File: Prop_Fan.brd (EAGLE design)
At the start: 160 x 100 mm, 77 parts, among them J1 500075-1517, SW1 EVQ-Q2203W, U1 P8X32A, U10 MAX31855KASA+, U2 FT230X, U3 LM22678TJ-5.0/NOPB, U6 ADP3338AKCZ-3.3-RL, U8 CAT24C512WI-GT3, U9 MAX31855KASA+, X1 ABLS3-6.000MHZ-D4Y-T

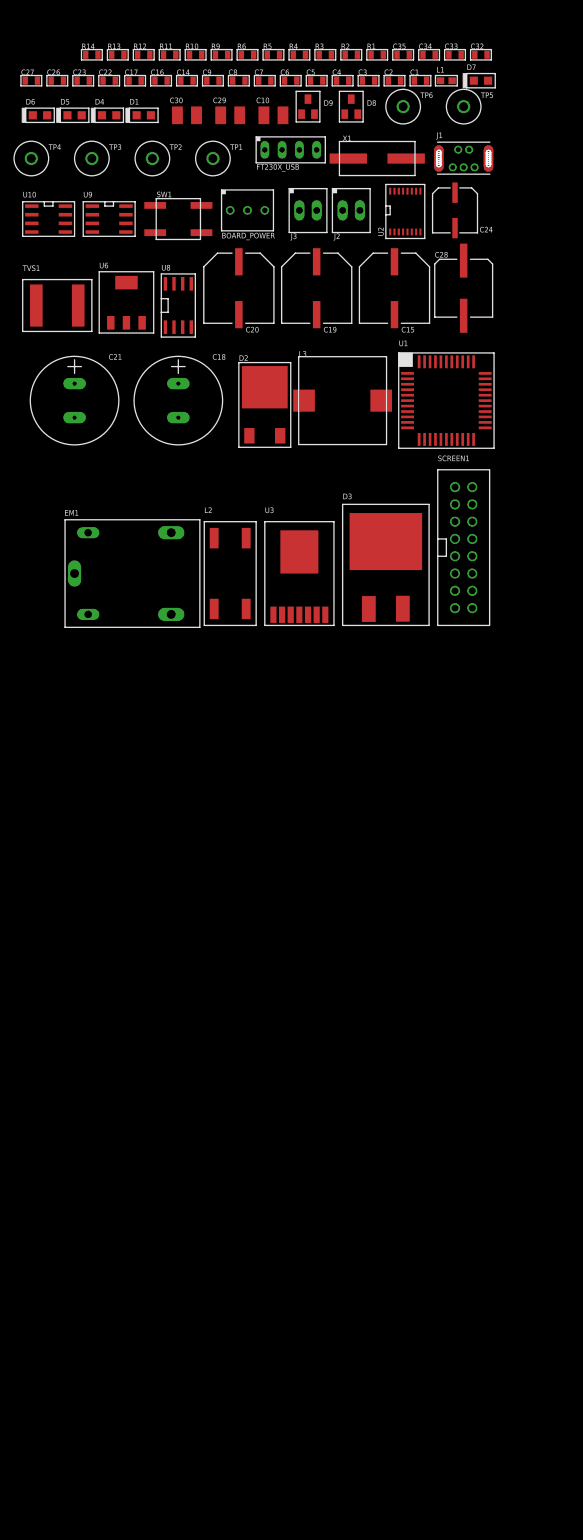
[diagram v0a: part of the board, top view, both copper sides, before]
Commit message: Need to add outputs.
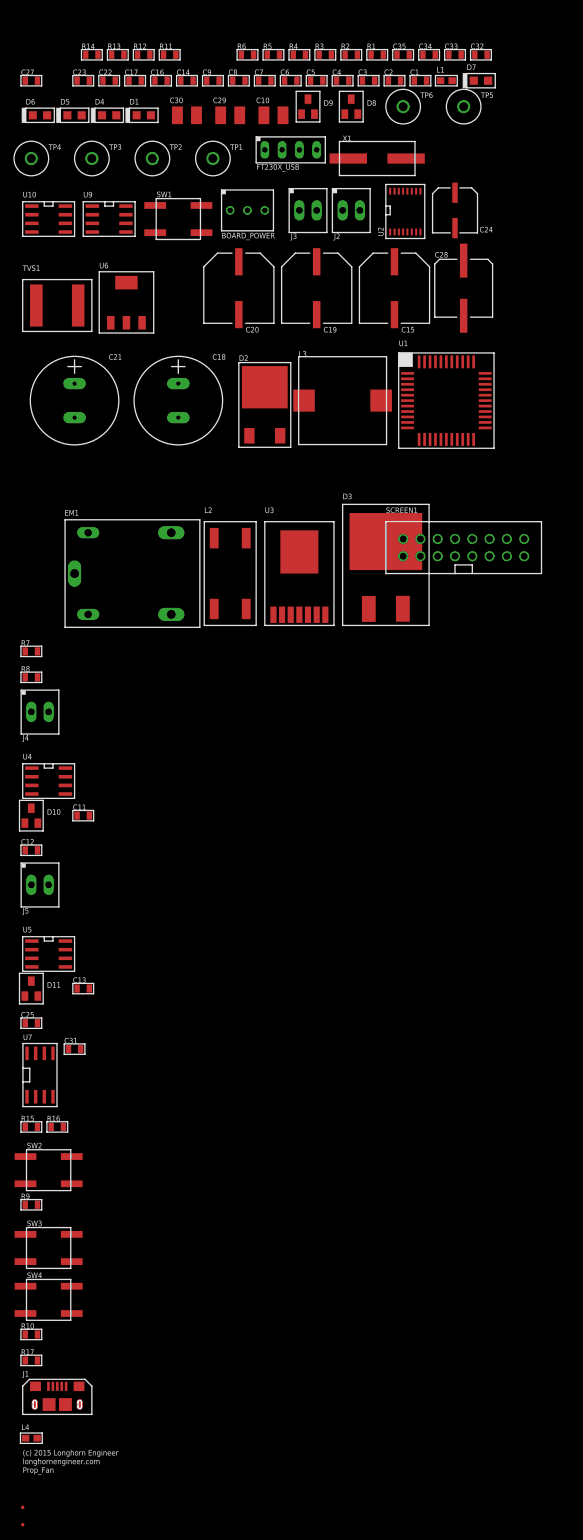
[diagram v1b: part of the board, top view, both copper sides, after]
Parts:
- removed C26: 0.1uF, PP_Passives:0805
- removed U8: CAT24C512WI-GT3, PP_DigitalIC:SOIC-8_W
- added C11, C12, C13, C25, C31: 0.1uF, PP_Passives:0805
- added D10, D11: NUP2105LT1G, PP_Passives:SOT-23
- added FID1, FID2: FIDUCIAL_0.5MM, MF_Aesthetics:FIDUCIAL_0.5MM
- added J4, J5: (no value), PP_Connectors:HEADER_01X02_PTH_SCREWTERM
- added L4: HI0603P600R-10, PP_Passives:0603
- added R15, R16, R17, R7, R8: 10K, PP_Passives:0805
- added SW2, SW3, SW4: EVQ-Q2203W, PP_Electromechanical:EVQ-Q2203W
- added U$1: LHE_FRAME, PP_Aesthetics:LHE_FRAME
- added U4, U5: MAX31855KASA+, PP_Sensors:SO-8
- added U7: CAT24C512WI-GT3, PP_DigitalIC:SOIC-8_W
- J1: value 500075-1517 -> (none); device PP_Connectors:500075-1517 -> MF_Connectors:MICROUSB-RIGHT
- SCREEN1: value ER-OLEDM032-1W -> ER-OLEDM2002-1Y
- moved J1 191.2 mm to (-77.5, -111.8)
- moved R10 189.5 mm to (-81.3, -102.9)
- moved R9 171.2 mm to (-81.3, -83.8)
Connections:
- removed net P22: U1.25
- removed net P23: U1.26
- removed net P6: U1.3
- removed net P7: U1.4
- removed net P8: U1.9
- new net N$3: J1.S1, J1.S2, J1.S3, J1.S4, J1.S5, J1.S6, J1.S7, J1.S8, L4.2
- new net SW_D: R9.2, SW4.1, SW4.2, U1.9
- new net SW_S: R10.2, SW3.1, SW3.2, U1.4
- new net SW_U: R17.2, SW2.1, SW2.2, U1.3
- new net T+_2: C12.1, D10.2, J4.1, U4.3
- new net T+_3: C25.1, D11.2, J5.1, U5.3
- new net T-_2: C12.2, D10.1, J4.2, U4.2
- new net T-_3: C25.2, D11.1, J5.2, U5.2
- new net TC_CS_2: U1.31, U4.6
- new net TC_CS_3: U1.32, U5.6
- net 3.3V: now also C11.1, C13.1, C31.1, R10.1, R15.2, R16.2, R17.1, R7.2, R8.2, R9.1, U4.4, U5.4, U7.8; no longer C26.1, R10.2, R9.2, U8.8
- net FT230X_D+: now also J1.3; no longer J1.D+
- net FT230X_D-: now also J1.2; no longer J1.D-
- net GND: now also C11.2, C13.2, C31.2, D10.3, D11.3, J1.5, L4.1, SCREEN1.P$15, SCREEN1.P$3, SCREEN1.P$4, SCREEN1.P$5, SCREEN1.P$6, SW2.3, SW2.4, SW3.3, SW3.4, SW4.3, SW4.4, U4.1, U5.1, U7.2, U7.3, U7.4, U7.7; no longer C26.2, J1.GND, J1.P$1, J1.P$2, J1.P$3, J1.P$4, SCREEN1.P$10, SCREEN1.P$14, SCREEN1.P$8, SCREEN1.P$9, U8.2, U8.3, U8.4, U8.7
- net SCL: now also R15.1, U7.6; no longer R9.1, U8.6
- net SCRN_CS: no longer SCREEN1.P$16
- net SCRN_RST: now also SCREEN1.P$14; no longer SCREEN1.P$15
- net SCRN_SCLK: now also R8.1, SCREEN1.P$10; no longer SCREEN1.P$4
- net SCRN_SDIN: now also R7.1, SCREEN1.P$8, SCREEN1.P$9; no longer SCREEN1.P$5
- net SDA: now also R16.1, U7.5; no longer R10.1, U8.5
- net TC_CS_0: now also U1.25; no longer U1.31
- net TC_CS_1: now also U1.26; no longer U1.32
- net TC_SCK: now also U4.5, U5.5
- net TC_SO: now also U4.7, U5.7
- net USB_V0: now also J1.1; no longer J1.5V

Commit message: Starting Layout.
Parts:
- removed D7: LG R971-KN-1, PP_LED:LED_0805
- removed FT230X_USB: (no value), PP_Connectors:HEADER_01X04_PTH
- removed R14: 330, PP_Passives:0805
- added R18: 0, PP_Passives:0805
- moved L4 271.0 mm to (104.4, 79.2), turned to 90 degrees
- moved J1 269.7 mm to (107.4, 84.6), turned to 180 degrees
- moved D1 180.4 mm to (115.6, 80.0), turned to 90 degrees
- moved C9 167.1 mm to (112.5, 79.2), turned to 90 degrees
- moved R6 165.1 mm to (115.6, 84.3), turned to 90 degrees
- moved C7 162.2 mm to (115.1, 73.9)
- moved R5 161.3 mm to (115.1, 72.1), turned to 180 degrees
- moved C6 158.7 mm to (115.1, 69.8)
- moved C8 153.4 mm to (102.6, 79.2), turned to 90 degrees
- moved R4 149.2 mm to (107.2, 79.2), turned to 90 degrees
- moved R3 147.2 mm to (109.0, 79.2), turned to 90 degrees
- moved U2 135.3 mm to (108.2, 73.4), turned to 270 degrees
- moved L1 131.1 mm to (110.7, 79.2), turned to 270 degrees
- moved R2 111.4 mm to (76.7, 75.4), turned to 90 degrees
- moved X1 108.6 mm to (74.9, 43.6), turned to 90 degrees
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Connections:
- removed net N$4: D7.ANODE, R14.1
- net 5V_PWR: now also R18.1
- net FT230X_D+: no longer FT230X_USB.3
- net FT230X_D-: no longer FT230X_USB.2
- net GND: no longer D7.CATHODE, FT230X_USB.4
- net USB_V0: no longer FT230X_USB.1
- net USB_V1: now also R18.2; no longer R14.2
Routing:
- net N$3: track 0.00 -> 21.9 mm
- net X1: track 0.00 -> 20.9 mm
- net X0: track 0.00 -> 20.9 mm
- net 3V3OUT: track 0.00 -> 14.9 mm
- net USBDP: track 0.00 -> 8.90 mm
- net USBDM: track 0.00 -> 8.80 mm
- net TXRX_LED: track 0.00 -> 7.62 mm
- net GND: track 0.00 -> 6.18 mm
- net FT230X_RST: track 0.00 -> 4.92 mm
- net USB_V0: track 0.00 -> 4.64 mm
- net FT230X_D-: track 0.00 -> 3.53 mm
- net FT230X_D+: track 0.00 -> 3.27 mm
- net N$1: track 0.00 -> 2.37 mm
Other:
- board size 160 x 100 mm -> 7.1 x 1.2 mm

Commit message: Working on power layout.
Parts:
- moved R18 264.8 mm to (134.5, 19.0), turned to 90 degrees
- moved R17 229.0 mm to (103.6, 28.5), turned to 270 degrees
- moved R10 220.0 mm to (103.4, 16.8), turned to 270 degrees
- moved SW2 217.2 mm to (110.2, 28.5)
- moved SW3 217.1 mm to (110.2, 16.8)
- moved SW4 215.1 mm to (110.2, 4.95)
- moved SW1 205.5 mm to (139.8, 11.7), turned to 180 degrees
- moved R9 204.9 mm to (103.4, 4.95), turned to 270 degrees
- moved C5 183.0 mm to (132.7, 19.0), turned to 270 degrees
- moved C34 169.0 mm to (-189.9, 110.8)
- moved C35 169.0 mm to (-193.7, 110.8)
- moved D8 169.0 mm to (-201.4, 103.2)
- moved R1 169.0 mm to (-197.6, 110.8)
- moved C1 169.0 mm to (-191.2, 107.0)
- moved C2 169.0 mm to (-195.0, 107.0)
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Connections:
- removed net P9: U1.10
- net GND: now also SCREEN1.P$10, SCREEN1.P$14, SCREEN1.P$8, SCREEN1.P$9; no longer SCREEN1.P$15, SCREEN1.P$3, SCREEN1.P$4, SCREEN1.P$5, SCREEN1.P$6
- net SCRN_CS: now also SCREEN1.P$16, U1.3
- net SCRN_RST: now also SCREEN1.P$15; no longer SCREEN1.P$14
- net SCRN_SCLK: now also SCREEN1.P$4; no longer SCREEN1.P$10
- net SCRN_SDIN: now also SCREEN1.P$5; no longer SCREEN1.P$8, SCREEN1.P$9
- net SW_D: now also U1.10; no longer U1.9
- net SW_S: now also U1.9; no longer U1.4
- net SW_U: now also U1.4; no longer U1.3
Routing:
- net CHASSIS_GND: track 0.00 -> 60.4 mm
- net 12V_BATT_ON: track 0.00 -> 33.1 mm
- net 12V_CLEAN: track 0.00 -> 22.7 mm
- net GND: track 6.18 -> 28.7 mm
- net USB_V1: track 0.00 -> 18.8 mm, vias 0 -> 2
- net USB_RST: track 0.00 -> 16.6 mm
- net 12V_BATT_SW: track 0.00 -> 16.4 mm
- net PROP_TX: track 0.00 -> 11.3 mm
- net 12V_AUX: track 0.00 -> 9.18 mm
- net PROP_RX: track 0.00 -> 8.97 mm
- net 12V_BATT: track 0.00 -> 7.18 mm
- net PROP_RES: track 0.00 -> 6.80 mm
- net RTS#: track 0.00 -> 4.88 mm
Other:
- board size 7.1 x 1.2 mm -> 100.5 x 34.5 mm

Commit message: Need to add optos.
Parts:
- removed EM1: G5LA-1A4-DC12, PP_Electromechanical:G5LA_PCBRELAY_SPDT
- removed L4: HI0603P600R-10, PP_Passives:0603
- removed R18: 0, PP_Passives:0805
- removed SCREEN1: ER-OLEDM2002-1Y, PP_Displays:ER-OLEDM032
- added C26, C38, C39, C40, C41: 0.1uF, PP_Passives:0805
- added C36: UWJ1C470MCL1GB, PP_Passives:6.3MM_CAP_SMD
- added C37: 47pF, PP_Passives:0805
- added D12, D7: NUP2105LT1G, PP_Passives:SOT-23
- added J6, J7: (no value), PP_Connectors:HEADER_01X02_PTH_SCREWTERM
- added LCD1: ER-OLEDM2002-1, PP_Displays:ER-OLEDM2002-1
- added R14: 10K, PP_Passives:0805
- added U11, U12: MAX31855KASA+, PP_Sensors:MAX31855_SO-8
- added U8: IP4234CZ6, PP_Passives:IP4234CZ6_SOT-457-6
- C6: value 0.1uF -> 47pF
- L1: value HI0603P600R-10 -> MI0603K300R-10
- R12: value 330 -> 390
- R3, R4: value 22 -> 27
- R5: value 10K -> 4.7K
- U1: value P8X32A -> P8X32A-Q44; device PP_DigitalIC:LQFP-44 -> MF_IC_Digital:LQFP44
- U10, U4, U5, U9: device PP_Sensors:SO-8 -> PP_Sensors:MAX31855_SO-8
- U2: value FT230X -> FT230XS; device PP_DigitalIC:SSOP-16 -> PP_DigitalIC:FT230X_QFN-16
- X1: value ABLS3-6.000MHZ-D4Y-T -> ABMM-6.000MHZ-B2-T; device PP_FreqCtrl:HC-49/US_SM -> MF_Frequency_Control:7MMX5MM
- moved J1 418.5 mm to (-222.0, -181.5), turned to 0 degrees
- moved X1 339.3 mm to (-207.5, -175.0), turned to 0 degrees
- moved U1 327.7 mm to (-220.0, -170.0)
- moved L1 6.35 mm to (136.0, 24.9), turned to 90 degrees
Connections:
- removed net 12V_AUX: BOARD_POWER.2, EM1.2
- removed net 12V_BATT_SW: D2.1, D2.3, EM1.3, TVS1.P$2
- removed net FT230X_RST: C7.1, R5.2, U1.42, U2.11
- removed net P20: U1.23
- removed net P21: U1.24
- removed net RTS#: C5.1, U2.2
- removed net SCRN_CS: SCREEN1.P$16, U1.2, U1.3
- removed net SCRN_SCLK: R8.1, SCREEN1.P$4, U1.43
- removed net SCRN_SDIN: R7.1, SCREEN1.P$5, U1.44
- removed net USB_V1: C8.1, C9.1, L1.2, R18.2, R6.2, U2.3
- new net !RTS: C5.1, U2.16
- new net N$10: C6.1, R4.2, U8.3
- new net N$6: C37.1, R3.2, U8.4
- new net P1: U1.42
- new net P5: U1.2
- new net P6: U1.3
- new net SCRN_SCL: LCD1.P$10, R8.1, U1.43
- new net SCRN_SDA: LCD1.P$8, LCD1.P$9, R7.1, U1.44
- new net TC_CS_4: U1.31, U5.6
- new net TC_CS_5: U1.32, U12.6
- new net VBUS_S: R14.1, R5.1, U2.14
- net 12V_BATT: now also D2.1, D2.3, TVS1.P$2; no longer EM1.1
- net 3.3V: now also C26.1, C36.POS, C38.1, C40.1, C8.1, C9.1, LCD1.P$2, R6.2, U11.4, U12.4, U2.10; no longer R5.1, SCREEN1.P$2
- net 3V3OUT: now also C7.1, U2.1, U2.8, U2.9; no longer C6.1, U2.10, U2.12
- net 5V_PWR: no longer R18.1
- net CHASSIS_GND: no longer EM1.5
- net FT230X_D+: now also U8.1; no longer R4.2
- net FT230X_D-: now also U8.6; no longer R3.2
- net GND: now also C26.2, C36.NEG, C37.2, C38.2, C40.2, D12.3, D7.3, L1.1, LCD1.P$1, LCD1.P$11, LCD1.P$12, LCD1.P$13, LCD1.P$15, LCD1.P$3, LCD1.P$4, LCD1.P$5, LCD1.P$6, LCD1.P$7, R14.2, U11.1, U12.1, U2.3, U2.PAD, U8.2, X1.P$2, X1.P$4; no longer L4.1, SCREEN1.P$1, SCREEN1.P$10, SCREEN1.P$11, SCREEN1.P$12, SCREEN1.P$13, SCREEN1.P$14, SCREEN1.P$7, SCREEN1.P$8, SCREEN1.P$9, U2.5
- net N$3: now also L1.2; no longer J1.S7, J1.S8, L4.2
- net PROP_RX: now also U2.2; no longer U2.4
- net PROP_TX: now also U2.15; no longer U2.1
- net SCRN_RST: now also LCD1.P$14; no longer SCREEN1.P$15
- net T+_1: now also C39.1, D7.2, J6.1, U11.3
- net T+_3: now also C41.1, D12.2, J7.1, U12.3
- net T-_1: now also C39.2, D7.1, J6.2, U11.2
- net T-_3: now also C41.2, D12.1, J7.2, U12.2
- net TC_CS_0: now also U1.23; no longer U1.25
- net TC_CS_1: now also U1.24; no longer U1.26
- net TC_CS_2: now also U1.25, U11.6; no longer U1.31, U4.6
- net TC_CS_3: now also U1.26, U4.6; no longer U1.32, U5.6
- net TC_SCK: now also U11.5, U12.5
- net TC_SO: now also U11.7, U12.7
- net TXRX_LED: now also U2.12; no longer U2.15
- net USBDM: now also U2.7; no longer U2.9
- net USBDP: now also U2.6; no longer U2.8
- net USB_V0: now also R5.2, U8.5; no longer L1.1
- net X0: now also X1.P$1; no longer X1.P$2
- net X1: now also X1.P$3; no longer X1.P$1
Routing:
- net X1: track 20.9 -> 0.00 mm
- net X0: track 20.9 -> 0.00 mm
- net N$3: track 21.9 -> 3.06 mm
- net USB_V1: track 18.8 -> 0.00 mm, vias 2 -> 0
- net 12V_BATT_SW: track 16.4 -> 0.00 mm
- net 3V3OUT: track 14.9 -> 0.00 mm
- net !RTS: track 0.00 -> 10.1 mm
- net 12V_AUX: track 9.18 -> 0.00 mm
- net 12V_BATT: track 7.18 -> 14.7 mm
- net PROP_TX: track 11.3 -> 16.7 mm
- net 12V_BATT_ON: track 33.1 -> 28.1 mm
- net FT230X_RST: track 4.92 -> 0.00 mm
- net RTS#: track 4.88 -> 0.00 mm
- net USB_V0: track 4.64 -> 0.00 mm
- net CHASSIS_GND: track 60.4 -> 56.6 mm
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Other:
- board size 100.5 x 34.5 mm -> 7.1 x 1.2 mm

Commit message: Working on Schematic. Need to add optos. Display Added.
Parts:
- removed BOARD_POWER: (no value), PP_Connectors:HEADER_01X03_PTH
- removed C13, C25, C26, C40, C41, C7, C8: 0.1uF, PP_Passives:0805
- removed C36: UWJ1C470MCL1GB, PP_Passives:6.3MM_CAP_SMD
- removed C37: 47pF, PP_Passives:0805
- removed C9: 1uF, PP_Passives:0805
- removed D1: LG R971-KN-1, PP_LED:LED_0805
- removed D11, D12: NUP2105LT1G, PP_Passives:SOT-23
- removed J5, J6, J7: (no value), PP_Connectors:HEADER_01X02_PTH_SCREWTERM
- removed L1: MI0603K300R-10, PP_Passives:0603
- removed LCD1: ER-OLEDM2002-1, PP_Displays:ER-OLEDM2002-1
- removed SW1: EVQ-Q2203W, PP_Electromechanical:EVQ-Q2203W
- removed U12: MAX31855KASA+, PP_Sensors:MAX31855_SO-8
- removed U2: FT230XS, PP_DigitalIC:FT230X_QFN-16
- removed U3: LM22678TJ-5.0/NOPB, PP_PowerIC:TO-263-7_TI
- removed U8: IP4234CZ6, PP_Passives:IP4234CZ6_SOT-457-6
- added BOARD_PWR: (no value), PP_Connectors:640454-3
- added DISP1: 61201621621, PP_Displays:CU40045-UW1J
- added PROP_TC: TC2030-FTDI-TTL-232R, PP_Connectors:TC2030
- added PROP_UART: (no value), PP_Connectors:2.54MM_01X06_PIN_HEADER
- added R18: 120, PP_Passives:0805
- C6: value 47pF -> 10uF
- D4, D5, D6: value LG R971-KN-1 -> MF-LED-0805-RED
- J1: value (none) -> 1546215-2; device MF_Connectors:MICROUSB-RIGHT -> PP_Connectors:1546215-2
- J2, J3, J4: value (none) -> 1546215-2; device PP_Connectors:HEADER_01X02_PTH_SCREWTERM -> PP_Connectors:1546215-2
- R14, R7, R8: value 10K -> 120
- R3, R4: value 27 -> 120
- R5: value 4.7K -> 120
- R6: value 330 -> 120
- U5: value MAX31855KASA+ -> LM22678TJ-5.0/NOPB; device PP_Sensors:MAX31855_SO-8 -> PP_PowerIC:LM22678_TO-263-EP-7
- U6: device PP_PowerIC:SOT-223 -> PP_PowerIC:ADP3338_SOT-223-3
- moved C6 513.2 mm to (-293.5, -248.5)
- moved R6 512.1 mm to (-293.5, -231.0), turned to 0 degrees
- moved R5 503.9 mm to (-293.5, -227.5), turned to 0 degrees
- moved R4 498.8 mm to (-293.5, -224.0), turned to 0 degrees
- moved R3 498.6 mm to (-293.5, -220.5), turned to 0 degrees
- moved J3 321.7 mm to (-277.0, -214.5)
- moved J2 321.2 mm to (-269.5, -214.5)
- moved R7 271.4 mm to (-293.5, -234.5)
- moved R8 271.2 mm to (-293.5, -238.0)
- moved J4 241.4 mm to (-284.5, -214.5)
- moved U5 168.7 mm to (-233.0, -191.5)
- moved R14 110.3 mm to (-293.5, -241.5)
- moved J1 50.9 mm to (-262.0, -213.0)
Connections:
- removed net !RTS: C5.1, U2.16
- removed net 3V3OUT: C7.1, U2.1, U2.8, U2.9
- removed net FT230X_D+: J1.3, U8.1
- removed net FT230X_D-: J1.2, U8.6
- removed net N$1: D1.ANODE, R6.1
- removed net N$10: C6.1, R4.2, U8.3
- removed net N$3: J1.S1, J1.S2, J1.S3, J1.S4, J1.S5, J1.S6, L1.2
- removed net N$6: C37.1, R3.2, U8.4
- removed net P1: U1.42
- removed net P10: U1.11
- removed net P5: U1.2
- removed net P6: U1.3
- removed net PROP_RX: U1.37, U2.2
- removed net PROP_TX: U1.38, U2.15
- removed net SCRN_RST: LCD1.P$14, U1.1
- removed net SCRN_SCL: LCD1.P$10, R8.1, U1.43
- removed net SCRN_SDA: LCD1.P$8, LCD1.P$9, R7.1, U1.44
- removed net T+_3: C25.1, C41.1, D11.2, D12.2, J5.1, J7.1, U12.3, U5.3
- removed net T-_3: C25.2, C41.2, D11.1, D12.1, J5.2, J7.2, U12.2, U5.2
- removed net TC_CS_4: U1.31, U5.6
- removed net TC_CS_5: U1.32, U12.6
- removed net TXRX_LED: D1.CATHODE, U2.12
- removed net USBDM: R3.1, U2.7
- removed net USBDP: R4.1, U2.6
- removed net USB_RST: C5.2, R2.1, SW1.1, SW1.2, U1.41
- removed net USB_V0: J1.1, R5.2, U8.5
- removed net VBUS_S: R14.1, R5.1, U2.14
- new net !RES!_PROP: C5.1, PROP_TC.P$6, PROP_UART.6
- new net D4: DISP1.P$4, R6.2
- new net D5: DISP1.P$3, R5.2
- new net D6: DISP1.P$2, R4.2
- new net D7: DISP1.P$1, R3.2
- new net E1: DISP1.P$9, R8.2
- new net E2: DISP1.P$15, R7.2
- new net P20: U1.23
- new net P21: U1.24
- new net PROP_D4: R6.1, U1.4
- new net PROP_D5: R5.1, U1.9
- new net PROP_D6: R4.1, U1.10
- new net PROP_D7: R3.1, U1.11
- new net PROP_E1: R8.1, U1.2
- new net PROP_E2: R7.1, U1.3
- new net PROP_R/W: R14.1, U1.1
- new net PROP_RS: R18.1, U1.44
- new net R/W: DISP1.P$10, R14.2
- new net RS: DISP1.P$11, R18.2
- new net RX_PROP: PROP_TC.P$4, PROP_UART.4, U1.38
- new net TX_PROP: PROP_TC.P$3, PROP_UART.5, U1.37
- net 12V_BATT: now also BOARD_PWR.P$1; no longer BOARD_POWER.1
- net 12V_CLEAN: now also U5.P$2; no longer U3.P$2
- net 3.3V: now also U6.2, U6.PAD; no longer C13.1, C26.1, C36.POS, C40.1, C8.1, C9.1, LCD1.P$2, R6.2, R7.2, R8.2, U12.4, U2.10, U5.4, U6.COM1, U6.COM2
- net 5V_PWR: now also C6.1, DISP1.P$14, U5.P$6, U6.3; no longer U3.P$6, U6.OUT
- net CHASSIS_GND: now also BOARD_PWR.P$3; no longer BOARD_POWER.3
- net GND: now also DISP1.P$13, DISP1.P$5, DISP1.P$6, DISP1.P$7, DISP1.P$8, PROP_TC.P$5, PROP_UART.1, U5.P$4, U5.PAD, U6.1; no longer C13.2, C26.2, C36.NEG, C37.2, C40.2, C7.2, C8.2, C9.2, D11.3, D12.3, J1.5, L1.1, LCD1.P$1, LCD1.P$11, LCD1.P$12, LCD1.P$13, LCD1.P$15, LCD1.P$3, LCD1.P$4, LCD1.P$5, LCD1.P$6, LCD1.P$7, R14.2, U12.1, U2.13, U2.3, U2.PAD, U3.P$4, U3.PAD, U5.1, U6.IN, U8.2
- net N$2: now also U5.P$3; no longer U3.P$3
- net N$5: now also U5.P$1; no longer U3.P$1
- net PROP_RES: now also C5.2, R2.1; no longer SW1.3, SW1.4
- net SW_D: now also U1.43; no longer U1.10
- net SW_S: now also U1.42; no longer U1.9
- net SW_U: now also U1.41; no longer U1.4
- net T+_0: now also J1.P$1; no longer J2.1
- net T+_1: now also J2.P$1, J3.P$1; no longer J3.1, J6.1
- net T+_2: now also J4.P$1; no longer J4.1
- net T-_0: now also J1.P$2; no longer J2.2
- net T-_1: now also J2.P$2, J3.P$2; no longer J3.2, J6.2
- net T-_2: now also J4.P$2; no longer J4.2
- net TC_CS_0: now also U1.25; no longer U1.23
- net TC_CS_1: now also U1.26; no longer U1.24
- net TC_CS_2: now also U1.31; no longer U1.25
- net TC_CS_3: now also U1.32; no longer U1.26
- net TC_SCK: no longer U12.5, U5.5
- net TC_SO: no longer U12.7, U5.7
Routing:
- net PROP_TX: track 16.7 -> 0.00 mm
- net USB_RST: track 16.6 -> 0.00 mm
- net PROP_RX: track 12.7 -> 0.00 mm
- net USBDM: track 12.6 -> 0.00 mm
- net TXRX_LED: track 11.0 -> 0.00 mm
- net USBDP: track 10.9 -> 0.00 mm
- net !RTS: track 10.1 -> 0.00 mm
- net GND: track 27.4 -> 22.6 mm
- net 12V_BATT: track 14.7 -> 9.96 mm
- net N$3: track 3.06 -> 0.00 mm
- net N$1: track 2.37 -> 0.00 mm
- net PROP_RES: track 6.80 -> 5.16 mm
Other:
- board outline removed

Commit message: Relay Control Hardware Complete.
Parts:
- added C7, C9: 0.1uF, PP_Passives:0805
- added R19, R20, R21, R22, R23, R24, R25, R26: 220, MF_Passives:R0603
- added R29, R30, R47, R48, R49, R50, R51, R52: 10K, MF_Passives:R0603
- added RELAYS, RELAYS1: 1-282834-0, PP_Connectors:1-282834-0
- added U12, U13, U17, U18, U19, U2, U3, U8: MF-DSC-SOT233-BSS138, MF_Discrete_Semiconductor:SOT-23-3
- added U14: CD74HC595M96, PP_DigitalIC:CD74HC595_SOIC-16
- added U16: CD74HC165M96, PP_DigitalIC:CD74HC165_SOIC-16
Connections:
- removed net P11: U1.12
- removed net P12: U1.13
- removed net P13: U1.14
- removed net P14: U1.15
- removed net P15: U1.16
- removed net P16: U1.19
- new net 165_CLK: U1.15, U16.2
- new net 165_DATA: U1.16, U16.9
- new net 165_LOAD: U1.19, U16.1
- new net 595_CLK: U1.12, U14.11
- new net 595_DATA: U1.13, U14.14
- new net 595_LAT: U1.14, U14.12
- new net IN_OPTO_1: U16.12
- new net IN_OPTO_2: U16.13
- new net IN_OPTO_3: U16.14
- new net IN_OPTO_4: U16.3
- new net IN_OPTO_5: U16.4
- new net IN_OPTO_6: U16.5
- new net IN_OPTO_7: U16.6
- new net N$11: R19.P$2, R29.P$2, U2.P$1
- new net N$12: R20.P$2, R30.P$2, U3.P$1
- new net N$13: R21.P$2, R47.P$2, U8.P$1
- new net N$14: R22.P$2, R48.P$2, U12.P$1
- new net N$15: R23.P$2, R49.P$2, U13.P$1
- new net N$16: R24.P$2, R50.P$2, U17.P$1
- new net N$17: R25.P$2, R51.P$2, U18.P$1
- new net N$18: R26.P$2, R52.P$2, U19.P$1
- new net OUT_OPTO_0: R19.P$1, U14.15
- new net OUT_OPTO_1: R20.P$1, U14.1
- new net OUT_OPTO_2: R21.P$1, U14.2
- new net OUT_OPTO_3: R22.P$1, U14.3
- new net OUT_OPTO_4: R23.P$1, U14.4
- new net OUT_OPTO_5: R24.P$1, U14.5
- new net OUT_OPTO_6: R25.P$1, U14.6
- new net OUT_OPTO_7: R26.P$1, U14.7
- new net P$1: R29.P$1, R30.P$1, R47.P$1, R48.P$1, R49.P$1, R50.P$1, R51.P$1, R52.P$1, U12.P$2, U13.P$2, U17.P$2, U18.P$2, U19.P$2, U2.P$2, U3.P$2, U8.P$2
- new net RLY_0: RELAYS.P$1, U2.P$3
- new net RLY_1: RELAYS.P$2, U3.P$3
- new net RLY_2: RELAYS.P$3, U8.P$3
- new net RLY_3: RELAYS.P$4, U12.P$3
- new net RLY_4: RELAYS.P$5, U13.P$3
- new net RLY_5: RELAYS.P$6, U17.P$3
- new net RLY_6: RELAYS.P$7, U18.P$3
- new net RLY_7: RELAYS.P$8, U19.P$3
- net 3.3V: now also C7.1, C9.1, U14.10, U14.16, U16.16
- net GND: now also C7.2, C9.2, U14.13, U14.8, U16.15, U16.8
